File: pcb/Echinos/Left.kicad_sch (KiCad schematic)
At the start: 29 parts, among them J1 USB_C_Receptacle_USB2.0, J2 FPC (PCB), J206 Conn_01x06_Pin, J4 FPC_VIK, J5 SATA-7p, U3 SRV05-4, U5 XC6210B332MR-G, U7 SRV05-4

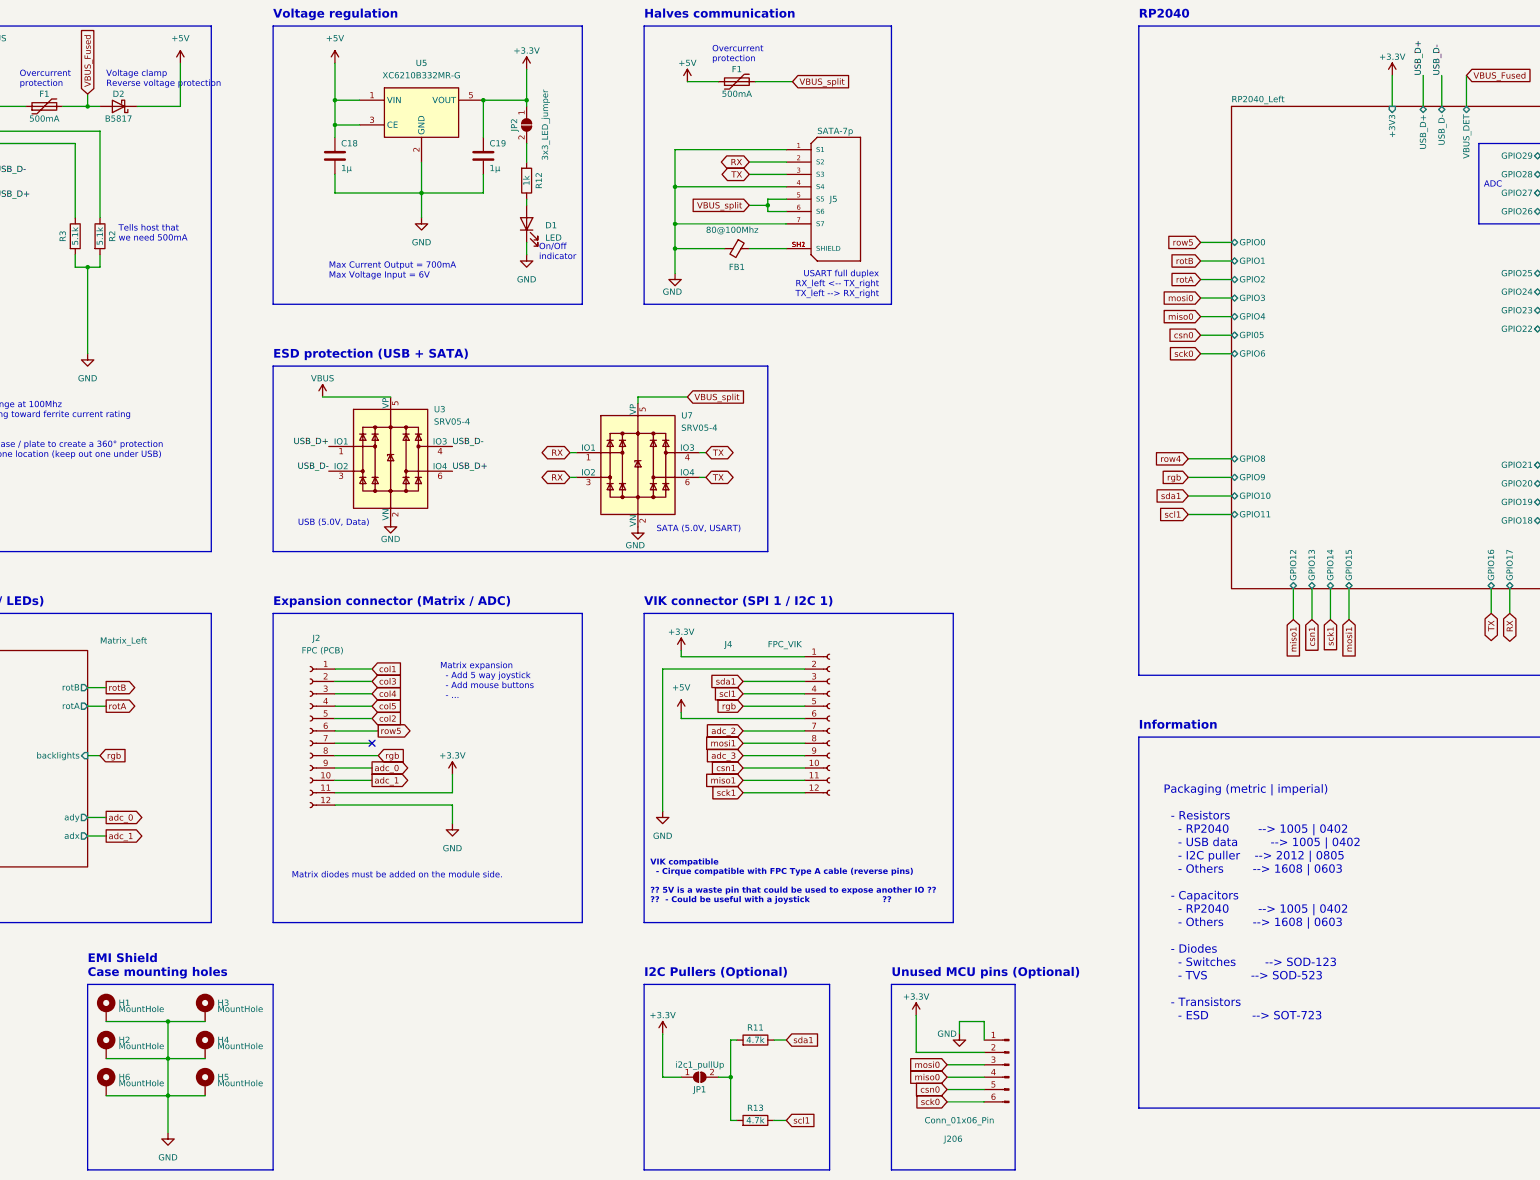
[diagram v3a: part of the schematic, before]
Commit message: ♻️ [PCB] - Fill / Check LCSC part number. Still some parts without a number:   - FPC connectors   - SATA connector   - Reset / Bootloader switches   - LED
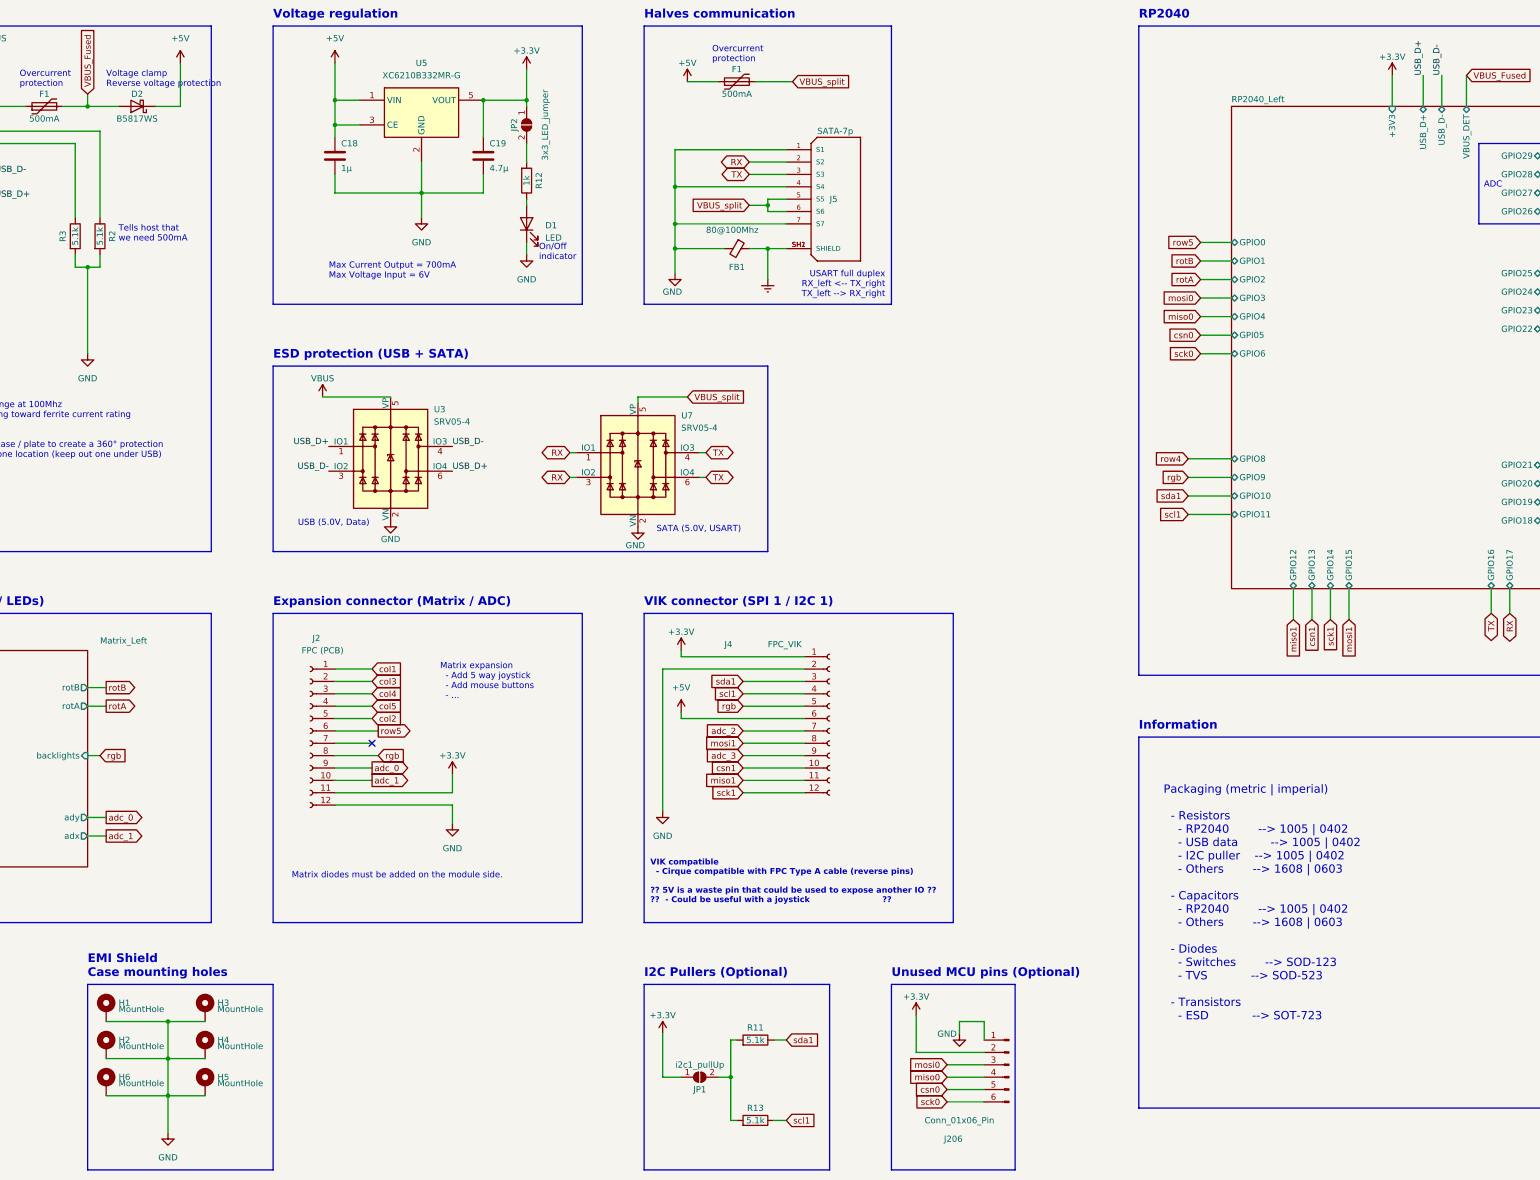
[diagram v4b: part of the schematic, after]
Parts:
- C18: LCSC C19666 -> C458913
- C19: value 1µ -> 4.7µ
- D2: value B5817 -> B5817WS
- J2: LCSC (none) -> TODO
- R11, R13: value 4.7k -> 5.1k; LCSC (none) -> C25905
- U3, U7: LCSC (none) -> C2972082
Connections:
- net Earth: now also FB1.1, J5.SH1 (SHIELD), J5.SH2 (SHIELD)
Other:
- note added: "Packaging (metric | imperial) - Resistors - RP2040 --> 1005 | 0402 - USB data --> 1005 | 0402 - I2C puller --> 1005 | 0402 - Others --> 1608 | 0603 - Capacitors - RP2040 --> 1005 | 0402 - Others --> 1608 | 0603 - Diodes - Switches --> SOD-123 - TVS --> SOD-523 - Transistors - ESD --> SOT-723"
- note removed: "Packaging (metric | imperial) - Resistors - RP2040 --> 1005 | 0402 - USB data --> 1005 | 0402 - I2C puller --> 2012 | 0805 - Others --> 1608 | 0603 - Capacitors - RP2040 --> 1005 | 0402 - Others --> 1608 | 0603 - Diodes - Switches --> SOD-123 - TVS --> SOD-523 - Transistors - ESD --> SOT-723"
- moved on the sheet: D2
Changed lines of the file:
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@@
   (junction (at 144.78 53.34) (diameter 0) (color 0 0 0 0)
+  )
+  (junction (at 215.9 64.77) (diameter 0) (color 0 0 0 0)
   )
   (junction (at 55.88 81.28) (diameter 0) (color 0 0 0 0)
@@
     (stroke (width 0) (type default))
   )
-  (wire (pts (xy 76.2 35.56) (xy 78.74 35.56))
+  (wire (pts (xy 76.2 35.56) (xy 82.55 35.56))
     (stroke (width 0) (type default))
   )
@@
     (stroke (width 0) (type default))
   )
-  (wire (pts (xy 86.36 35.56) (xy 95.25 35.56))
+  (wire (pts (xy 90.17 35.56) (xy 95.25 35.56))
     (stroke (width 0) (type default))
   )
@@
     (stroke (width 0) (type default))
   )
+  (wire (pts (xy 215.9 64.77) (xy 215.9 71.12))
+    (stroke (width 0) (type default))
+  )
   (wire (pts (xy 95.25 26.67) (xy 95.25 35.56))
     (stroke (width 0) (type default))
@@
     (stroke (width 0) (type default))
   )
+  (wire (pts (xy 215.9 64.77) (xy 219.71 64.77))
+    (stroke (width 0) (type default))
+  )
   (wire (pts (xy 217.17 243.84) (xy 219.71 243.84))
     (stroke (width 0) (type default))
@@
     (stroke (width 0) (type default))
   )
-  (wire (pts (xy 212.09 64.77) (xy 219.71 64.77))
+  (wire (pts (xy 212.09 64.77) (xy 215.9 64.77))
     (stroke (width 0) (type default))
   )
@@
     (effects (font (size 1.27 1.27)) (justify left bottom))
   )
-  (text "Packaging (metric | imperial)\n\n  - Resistors\n	- RP2040		--> 1005 | 0402\n	- USB data 		--> 1005 | 0402\n	- I2C puller	--> 2012 | 0805\n	- Others		--> 1608 | 0603\n\n  - Capacitors\n	- RP2040		--> 1005 | 0402\n	- Others		--> 1608 | 0603\n\n  - Diodes\n	- Switches		--> SOD-123\n	- TVS			--> SOD-523\n\n  - Transistors\n	- ESD			--> SOT-723"
+  (text "Packaging (metric | imperial)\n\n  - Resistors\n	- RP2040		--> 1005 | 0402\n	- USB data 		--> 1005 | 0402\n	- I2C puller	--> 1005 | 0402\n	- Others		--> 1608 | 0603\n\n  - Capacitors\n	- RP2040		--> 1005 | 0402\n	- Others		--> 1608 | 0603\n\n  - Diodes\n	- Switches		--> SOD-123\n	- TVS			--> SOD-523\n\n  - Transistors\n	- ESD			--> SOT-723"
     (at 297.18 223.52 0)
     (effects (font (size 1.7 1.7)) (justify left bottom))
@@
   )
   (text "USART full duplex\nRX_left <-- TX_right\nTX_left --> RX_right"
-    (at 238.76 74.93 0)
+    (at 240.03 74.93 0)
     (effects (font (size 1.27 1.27)) (justify right bottom) (href "https://github.com/qmk/qmk_firmware/blob/master/docs/serial_driver.md#usart-full-duplex"))
   )
@@
       (effects (font (size 1.27 1.27)) hide)
     )
-    (property "Datasheet" "http://www.onsemi.com/pub/Collateral/SRV05-4-D.PDF" (at 189.23 109.22 0)
+    (property "Datasheet" "https://datasheet.lcsc.com/lcsc/2309211436_DOWO-SRV05-4_C2972082.pdf" (at 189.23 109.22 0)
+      (effects (font (size 1.27 1.27)) hide)
+    )
+    (property "LCSC" "C2972082" (at 189.23 109.22 0)
       (effects (font (size 1.27 1.27)) hide)
     )
@@
       (effects (font (size 1.27 1.27)) hide)
     )
-    (property "Datasheet" "http://www.onsemi.com/pub/Collateral/SRV05-4-D.PDF" (at 138.43 107.95 0)
+    (property "Datasheet" "https://datasheet.lcsc.com/lcsc/2309211436_DOWO-SRV05-4_C2972082.pdf" (at 138.43 107.95 0)
+      (effects (font (size 1.27 1.27)) hide)
+    )
+    (property "LCSC" "C2972082" (at 138.43 107.95 0)
       (effects (font (size 1.27 1.27)) hide)
     )
@@
       (effects (font (size 1.27 1.27)))
     )
-    (property "Value" "4.7k" (at 213.36 227.33 90)
+    (property "Value" "5.1k" (at 213.36 227.33 90)
       (effects (font (size 1.27 1.27)))
     )
@@
       (effects (font (size 1.27 1.27)) hide)
     )
-    (property "LCSC" "" (at 213.36 227.33 0)
+    (property "LCSC" "C25905" (at 213.36 227.33 0)
       (effects (font (size 1.27 1.27)) hide)
     )
@@
     )
   )
-  (symbol (lib_id "Device:D_Schottky") (at 82.55 35.56 180) (unit 1)
-    (in_bom yes) (on_board yes) (dnp no)
-    (property "Reference" "D2" (at 82.55 33.02 0)
-      (effects (font (size 1.27 1.27)))
-    )
-    (property "Value" "B5817" (at 82.55 38.1 0)
-      (effects (font (size 1.27 1.27)))
-    )
-    (property "Footprint" "Diode_SMD:D_SOD-323_HandSoldering" (at 82.55 35.56 0)
-      (effects (font (size 1.27 1.27)) hide)
-    )
-    (property "Datasheet" "~" (at 82.55 35.56 0)
-      (effects (font (size 1.27 1.27)) hide)
-    )
-    (property "LCSC" "C123899" (at 82.55 35.56 0)
+  (symbol (lib_id "Device:D_Schottky") (at 86.36 35.56 180) (unit 1)
+    (in_bom yes) (on_board yes) (dnp no)
+    (property "Reference" "D2" (at 86.36 33.02 0)
+      (effects (font (size 1.27 1.27)))
+    )
+    (property "Value" "B5817WS" (at 86.36 38.1 0)
+      (effects (font (size 1.27 1.27)))
+    )
+    (property "Footprint" "Diode_SMD:D_SOD-323_HandSoldering" (at 86.36 35.56 0)
+      (effects (font (size 1.27 1.27)) hide)
+    )
+    (property "Datasheet" "~" (at 86.36 35.56 0)
+      (effects (font (size 1.27 1.27)) hide)
+    )
+    (property "LCSC" "C123899" (at 86.36 35.56 0)
       (effects (font (size 1.27 1.27)) hide)
     )
@@
       (effects (font (size 1.27 1.27)) hide)
     )
-    (property "LCSC" "" (at 121.92 163.83 0)
+    (property "LCSC" "TODO" (at 121.92 163.83 0)
       (effects (font (size 1.27 1.27)) hide)
     )
@@
       (effects (font (size 1.27 1.27)) hide)
     )
-    (property "LCSC" "C19666" (at 127 45.72 0)
+    (property "LCSC" "C458913" (at 127 45.72 0)
       (effects (font (size 1.27 1.27)) hide)
     )
@@
         (path "/7353e96a-343a-4876-b497-b1d205a14d97"
           (reference "#PWR08") (unit 1)
+        )
+      )
+    )
+  )
+  (symbol (lib_id "power:Earth") (at 215.9 71.12 0) (unit 1)
+    (in_bom yes) (on_board yes) (dnp no) (fields_autoplaced)
+    (property "Reference" "#PWR021" (at 215.9 77.47 0)
+      (effects (font (size 1.27 1.27)) hide)
+    )
+    (property "Value" "Earth" (at 215.9 74.93 0)
+      (effects (font (size 1.27 1.27)) hide)
+    )
+    (property "Footprint" "" (at 215.9 71.12 0)
+      (effects (font (size 1.27 1.27)) hide)
+    )
+    (property "Datasheet" "~" (at 215.9 71.12 0)
+      (effects (font (size 1.27 1.27)) hide)
+    )
+    (pin "1")
+    (instances
+      (project "Echinos"
+        (path "/5bd3006d-ec09-4ffb-bec3-03fa5613b46a/82089e05-aeac-4bc0-b466-29ce28ef1ab1"
+          (reference "#PWR021") (unit 1)
         )
       )
@@
       (effects (font (size 1.27 1.27)) (justify left))
     )
-    (property "Value" "1µ" (at 158.75 48.26 0)
+    (property "Value" "4.7µ" (at 158.75 48.26 0)
       (effects (font (size 1.27 1.27)) (justify left))
     )
@@
       (effects (font (size 1.27 1.27)))
     )
-    (property "Value" "4.7k" (at 213.36 243.84 90)
+    (property "Value" "5.1k" (at 213.36 243.84 90)
       (effects (font (size 1.27 1.27)))
     )
@@
       (effects (font (size 1.27 1.27)) hide)
     )
-    (property "LCSC" "" (at 213.36 243.84 0)
-      (effects (font (size 1.27 1.27)) hide)
-    )
+    (property "LCSC" "C25905" (at 213.36 243.84 0)
+      (effects (font (size 1.27 1.27)) hide)
+    )

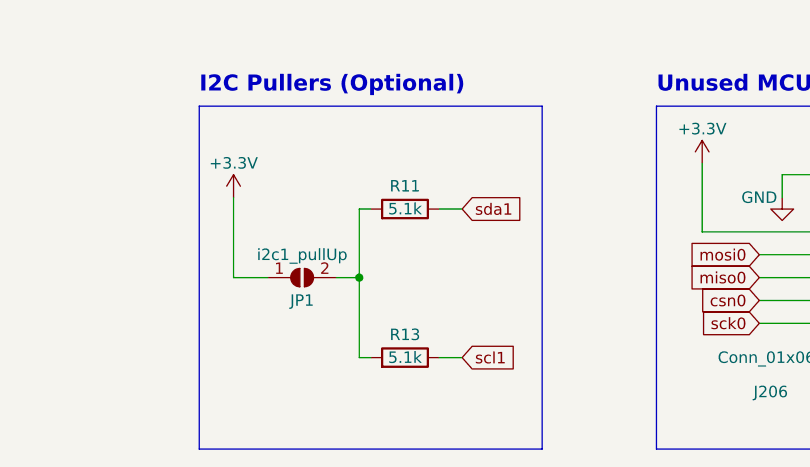
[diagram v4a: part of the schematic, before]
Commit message: ♻️ [Case] - Use 4.7k resistance as I2C pull-up resistors instead of 5.1k
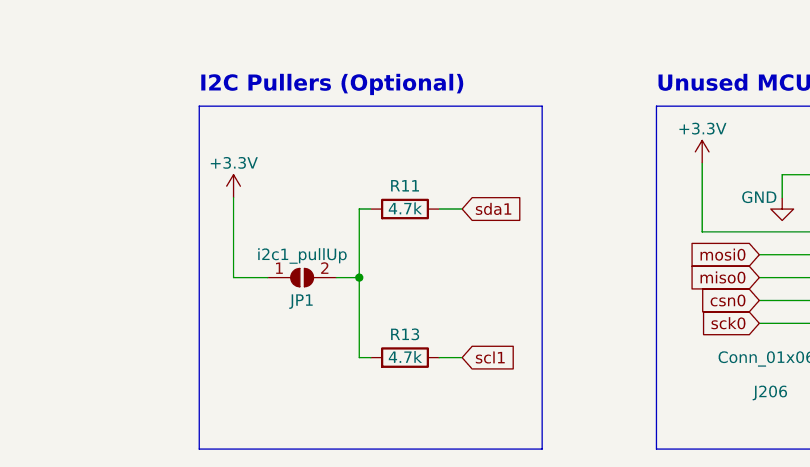
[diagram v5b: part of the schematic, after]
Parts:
- R11, R13: value 5.1k -> 4.7k; LCSC C25905 -> C25900
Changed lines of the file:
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@@
       (effects (font (size 1.27 1.27)))
     )
-    (property "Value" "5.1k" (at 213.36 227.33 90)
+    (property "Value" "4.7k" (at 213.36 227.33 90)
       (effects (font (size 1.27 1.27)))
     )
@@
       (effects (font (size 1.27 1.27)) hide)
     )
-    (property "LCSC" "C25905" (at 213.36 227.33 0)
+    (property "LCSC" "C25900" (at 213.36 227.33 0)
       (effects (font (size 1.27 1.27)) hide)
     )
@@
       (effects (font (size 1.27 1.27)))
     )
-    (property "Value" "5.1k" (at 213.36 243.84 90)
+    (property "Value" "4.7k" (at 213.36 243.84 90)
       (effects (font (size 1.27 1.27)))
     )
@@
       (effects (font (size 1.27 1.27)) hide)
     )
-    (property "LCSC" "C25905" (at 213.36 243.84 0)
-      (effects (font (size 1.27 1.27)) hide)
-    )
+    (property "LCSC" "C25900" (at 213.36 243.84 0)
+      (effects (font (size 1.27 1.27)) hide)
+    )
